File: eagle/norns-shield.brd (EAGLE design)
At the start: 85.1 x 80 mm, 77 parts, among them J1 TRS-IN, J2 TRS-OUT, J3 ISP-ROW, Q1 ASFL-12.288mhz, SW1 PVA1, SW2 PVA1, SW3 PVA1, U1 CS4270, X1 RASPI_BOARD_B+#_E3

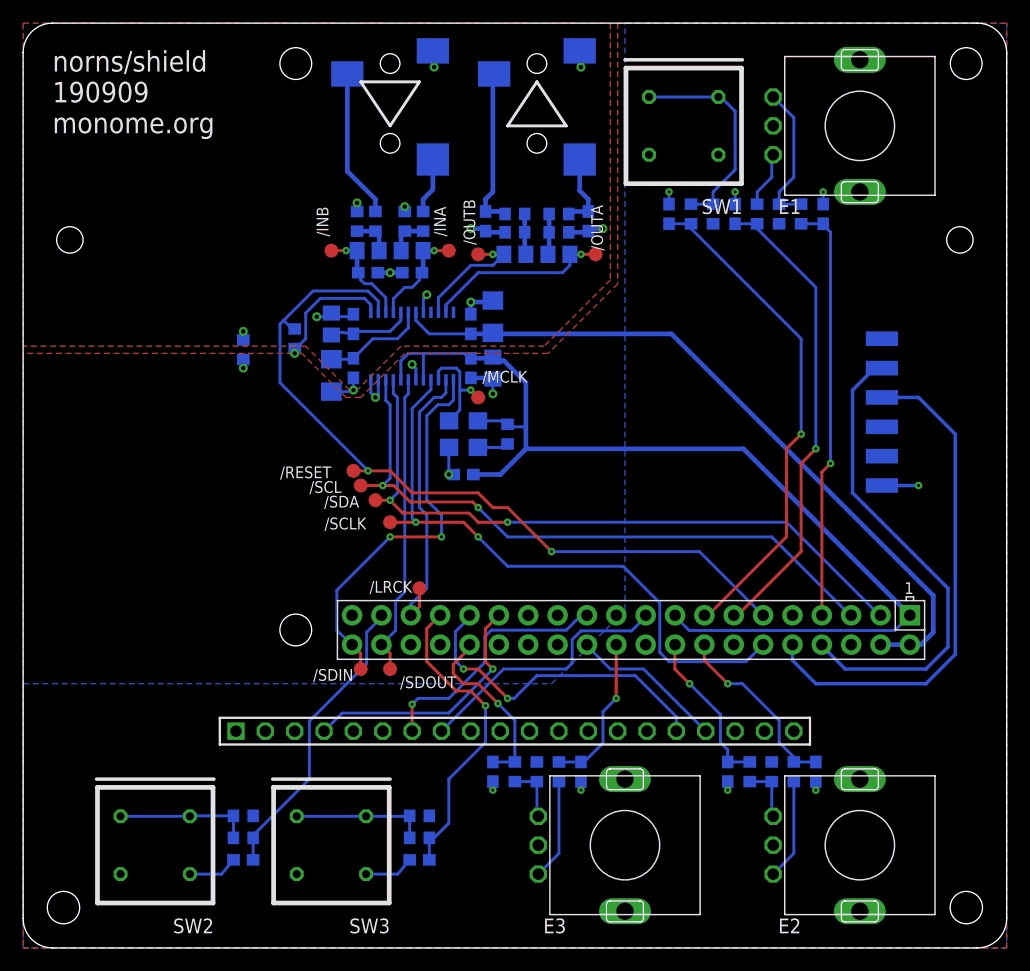
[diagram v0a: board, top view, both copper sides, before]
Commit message: 191021, add pullups to encoders
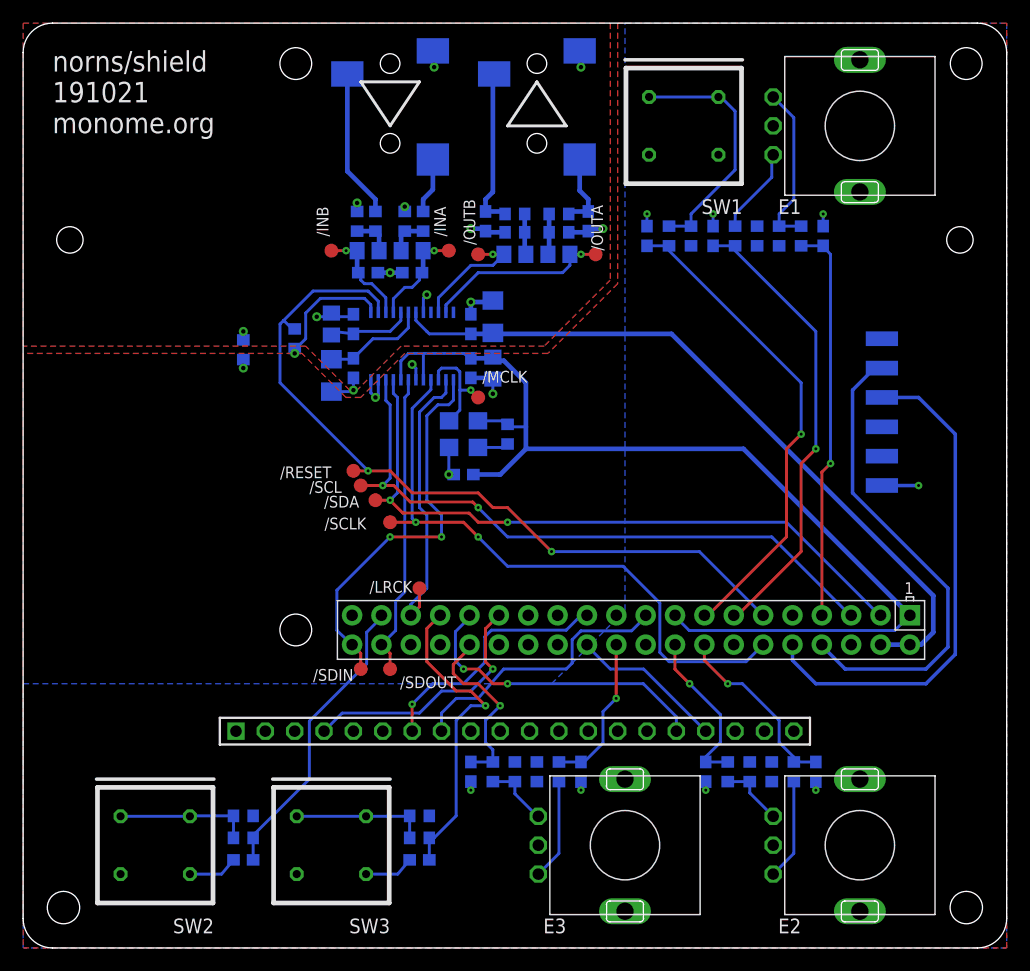
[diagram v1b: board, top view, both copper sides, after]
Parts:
- added R2, R3, R4: 10k, rcl:R0603
- moved C36 2.69 mm to (59.7, 37.5)
- moved C44 2.69 mm to (54.0, 37.5)
- moved R26 2.69 mm to (61.6, 37.5)
- moved R44 2.69 mm to (57.8, 37.5)
- moved R45 2.69 mm to (55.9, 37.5)
- moved C38 1.91 mm to (59.1, -8.89)
- moved C41 1.91 mm to (38.7, -8.89)
- moved R34 1.91 mm to (61.0, -8.89)
- moved R40 1.91 mm to (40.6, -8.89)
- moved R41 1.91 mm to (42.5, -8.89)
- moved C35 1.90 mm to (69.2, 37.5)
- moved R28 1.90 mm to (67.3, 37.5)
- moved R29 1.90 mm to (65.4, 37.5)
- moved R35 1.90 mm to (62.9, -8.89)
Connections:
- net +3V3: now also R2.2, R3.2, R4.2
- net N$19: now also R2.1
- net N$22: now also R3.1
- net N$27: now also R4.1
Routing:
- net N$19: track 4.84 -> 7.53 mm
- net N$2: track 18.7 -> 21.4 mm
- net N$18: track 12.4 -> 14.3 mm
- net A1: track 36.3 -> 34.4 mm
- net O_RESET: track 28.4 -> 26.8 mm
- net B1: track 41.0 -> 39.9 mm
- net K1: track 43.4 -> 42.3 mm
- net MOSI: track 23.1 -> 24.1 mm
- net N$28: track 4.95 -> 5.90 mm
- net N$25: track 4.95 -> 5.74 mm
- net K3: track 26.7 -> 27.5 mm
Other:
- board text added: "norns/shield 191021 monome.org"
- board text removed: "norns/shield 190909 monome.org"
